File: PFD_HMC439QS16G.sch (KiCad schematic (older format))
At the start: 74 parts, among them J1 REF, J2 IN, J3 Error_Out, J4 C64AC, J5 Fast_Out, U1 HMC439QS16G, U2 LT3045EMSE, U3 LT3094EMSE, U4 ADA4896-2ARMZ, U5 ADA4896-2ARMZ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

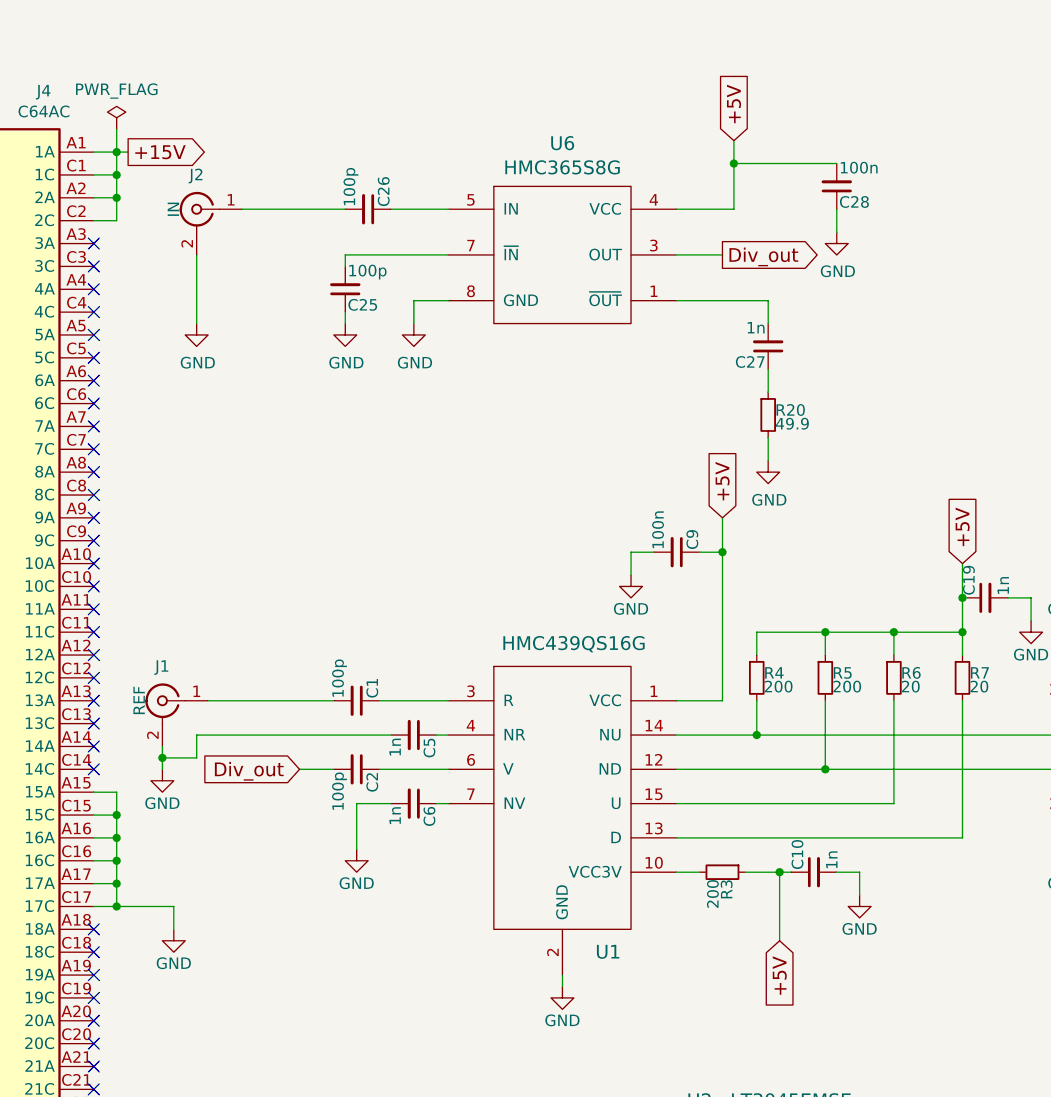
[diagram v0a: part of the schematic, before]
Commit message: Remove HMC365 frequency divider
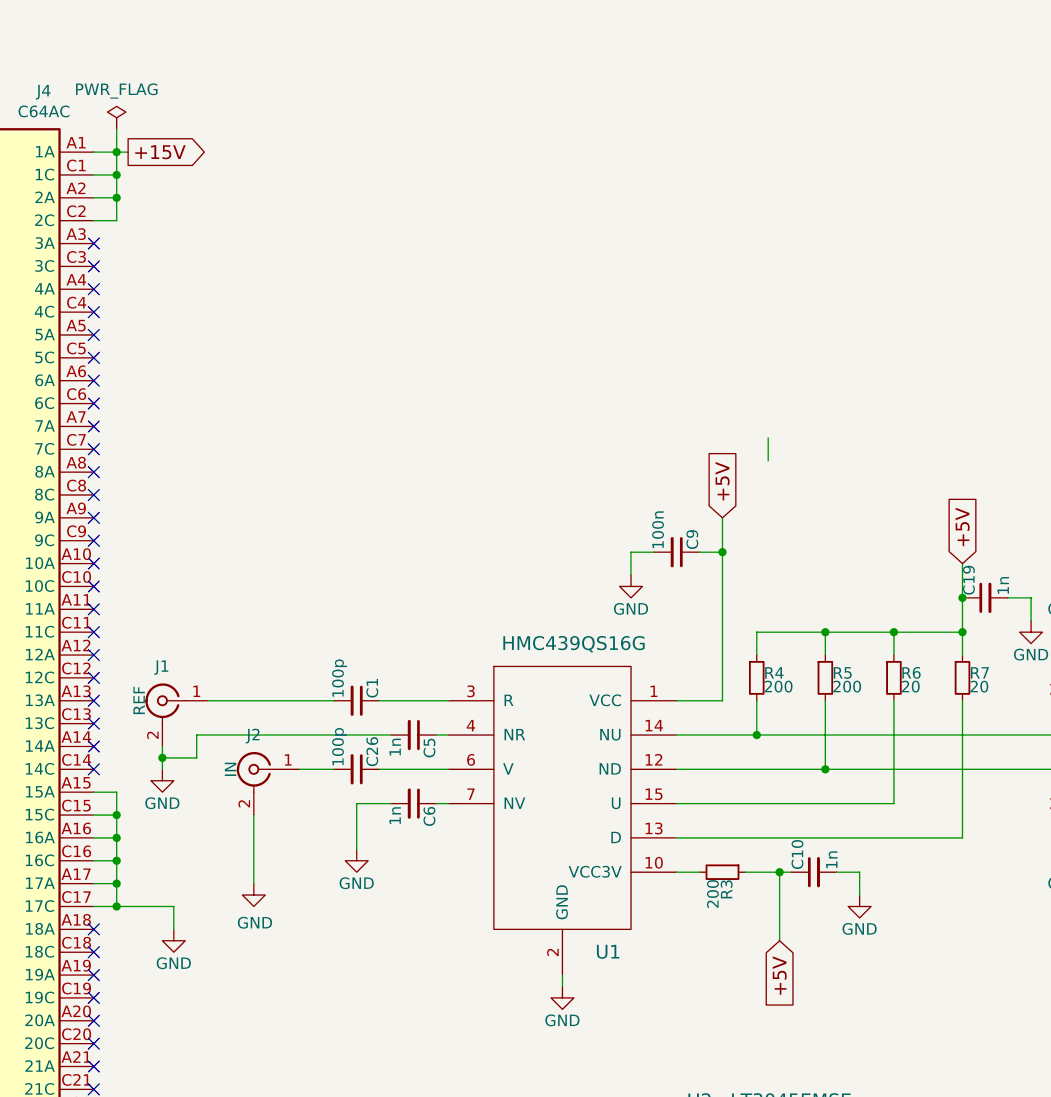
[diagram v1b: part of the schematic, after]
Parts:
- removed C2, C25: 100p, Capacitor_SMD:C_0402_1005Metric, symbol Device:C_Small
- removed C27: 1n, Capacitor_SMD:C_0603_1608Metric, symbol Device:C_Small
- removed C28: 100n, Capacitor_SMD:C_0603_1608Metric, symbol Device:C_Small
- removed R20: 49.9, Resistor_SMD:R_0603_1608Metric, symbol Device:R_Small
- removed U6: HMC365S8G, Package_SO:SOIC-8-1EP_3.9x4.9mm_P1.27mm_EP2.41x3.81mm, symbol Linear-Technology:HMC365S8G
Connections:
- net at U1.6 (V): now also C26.1
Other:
- moved on the sheet: C26, J2
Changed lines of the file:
@@
 Sheet 1 1
 Title "HMC439 Phase-Frequency Detector"
-Date "2021-03-18"
-Rev "1.2"
+Date "2021-08-22"
+Rev "1.2b"
 Comp "APQ"
 Comment1 "Tilman Preuschoff"
@@
 $EndComp
 $Comp
-L Device:C_Small C2
-U 1 1 5C6B19B9
-P 2150 3800
-F 0 "C2" H 2160 3870 50  0000 L CNN
-F 1 "100p" H 2160 3720 50  0000 L CNN
-F 2 "Capacitor_SMD:C_0402_1005Metric" H 2150 3800 50  0001 C CNN
-F 3 "" H 2150 3800 50  0001 C CNN
-	1    2150 3800
-	0    1    1    0
-$EndComp
-$Comp
 L Device:C_Small C6
 U 1 1 5C6B1ADB
@@
 L Connector:Conn_Coaxial J2
 U 1 1 5C6B26F6
-P 1450 1350
-F 0 "J2" H 1450 1500 50  0000 C CNN
-F 1 "IN" V 1550 1350 50  0000 C CNN
-F 2 "Connector_Coaxial:SMA_Amphenol_901-144_Vertical" H 1450 1350 50  0001 C CNN
-F 3 "" H 1450 1350 50  0001 C CNN
-	1    1450 1350
+P 1700 3800
+F 0 "J2" H 1700 3950 50  0000 C CNN
+F 1 "IN" V 1800 3800 50  0000 C CNN
+F 2 "Connector_Coaxial:SMA_Amphenol_901-144_Vertical" H 1700 3800 50  0001 C CNN
+F 3 "" H 1700 3800 50  0001 C CNN
+	1    1700 3800
 	-1   0    0    -1
 $EndComp
@@
 	9800 1300 9800 1900
 $Comp
-L Linear-Technology:HMC365S8G U6
-U 1 1 6058F7BE
-P 3050 1700
-F 0 "U6" H 3050 2337 60  0000 C CNN
-F 1 "HMC365S8G" H 3050 2231 60  0000 C CNN
-F 2 "Package_SO:SOIC-8-1EP_3.9x4.9mm_P1.27mm_EP2.41x3.81mm" H 3050 1700 60  0001 C CNN
-F 3 "https://www.analog.com/media/en/technical-documentation/data-sheets/HMC365S8G.pdf" H 3050 1700 60  0001 C CNN
-	1    3050 1700
-	1    0    0    -1
-$EndComp
-$Comp
 L Device:C_Small C26
 U 1 1 605ABF87
-P 2200 1350
-F 0 "C26" H 2210 1420 50  0000 L CNN
-F 1 "100p" H 2210 1270 50  0000 L CNN
-F 2 "Capacitor_SMD:C_0402_1005Metric" H 2200 1350 50  0001 C CNN
-F 3 "" H 2200 1350 50  0001 C CNN
-	1    2200 1350
+P 2150 3800
+F 0 "C26" H 2160 3870 50  0000 L CNN
+F 1 "100p" H 2160 3720 50  0000 L CNN
+F 2 "Capacitor_SMD:C_0402_1005Metric" H 2150 3800 50  0001 C CNN
+F 3 "" H 2150 3800 50  0001 C CNN
+	1    2150 3800
 	0    1    -1   0
-$EndComp
-$Comp
-L power:GND #PWR0105
-U 1 1 605AD690
-P 2400 1850
-F 0 "#PWR0105" H 2400 1600 50  0001 C CNN
-F 1 "GND" H 2405 1677 50  0000 C CNN
-F 2 "" H 2400 1850 50  0001 C CNN
-F 3 "" H 2400 1850 50  0001 C CNN
-	1    2400 1850
-	1    0    0    -1
-$EndComp
-$Comp
-L power:GND #PWR0106
-U 1 1 605ADE4E
-P 2100 1850
-F 0 "#PWR0106" H 2100 1600 50  0001 C CNN
-F 1 "GND" H 2105 1677 50  0000 C CNN
-F 2 "" H 2100 1850 50  0001 C CNN
-F 3 "" H 2100 1850 50  0001 C CNN
-	1    2100 1850
-	1    0    0    -1
 $EndComp
 $Comp
 L power:GND #PWR0110
 U 1 1 605BA26B
-P 1450 1850
-F 0 "#PWR0110" H 1450 1600 50  0001 C CNN
-F 1 "GND" H 1455 1677 50  0000 C CNN
-F 2 "" H 1450 1850 50  0001 C CNN
-F 3 "" H 1450 1850 50  0001 C CNN
-	1    1450 1850
-	1    0    0    -1
-$EndComp
-Wire Wire Line
-	1450 1550 1450 1850
-Wire Wire Line
-	2400 1750 2400 1850
-Wire Wire Line
-	2400 1750 2550 1750
-$Comp
-L Device:C_Small C25
-U 1 1 605DBB01
-P 2100 1700
-F 0 "C25" H 2110 1770 50  0000 L CNN
-F 1 "100p" H 2110 1620 50  0000 L CNN
-F 2 "Capacitor_SMD:C_0402_1005Metric" H 2100 1700 50  0001 C CNN
-F 3 "" H 2100 1700 50  0001 C CNN
-	1    2100 1700
-	1    0    0    1
-$EndComp
-Wire Wire Line
-	2550 1550 2100 1550
-Wire Wire Line
-	2100 1550 2100 1600
-Wire Wire Line
-	2100 1850 2100 1800
-Wire Wire Line
-	1650 1350 2100 1350
-Wire Wire Line
-	2300 1350 2550 1350
+P 1700 4300
+F 0 "#PWR0110" H 1700 4050 50  0001 C CNN
+F 1 "GND" H 1705 4127 50  0000 C CNN
+F 2 "" H 1700 4300 50  0001 C CNN
+F 3 "" H 1700 4300 50  0001 C CNN
+	1    1700 4300
+	1    0    0    -1
+$EndComp
+Wire Wire Line
+	1700 4000 1700 4300
 Wire Wire Line
 	1300 3700 1300 3750
@@
 Wire Wire Line
 	1300 3750 1300 3800
-Text GLabel 3800 1050 1    60   Input ~ 0
-+5V
-$Comp
-L Device:C_Small C28
-U 1 1 60639204
-P 4250 1250
-F 0 "C28" H 4260 1320 50  0000 L CNN
-F 1 "100n" H 4260 1170 50  0000 L CNN
-F 2 "Capacitor_SMD:C_0603_1608Metric" H 4250 1250 50  0001 C CNN
-F 3 "" H 4250 1250 50  0001 C CNN
-	1    4250 1250
-	1    0    0    1
-$EndComp
-Wire Wire Line
-	3800 1050 3800 1150
-Wire Wire Line
-	3800 1350 3550 1350
-Wire Wire Line
-	3800 1150 4250 1150
-Connection ~ 3800 1150
-Wire Wire Line
-	3800 1150 3800 1350
-$Comp
-L power:GND #PWR0111
-U 1 1 60661DA4
-P 4250 1450
-F 0 "#PWR0111" H 4250 1200 50  0001 C CNN
-F 1 "GND" H 4255 1277 50  0000 C CNN
-F 2 "" H 4250 1450 50  0001 C CNN
-F 3 "" H 4250 1450 50  0001 C CNN
-	1    4250 1450
-	1    0    0    -1
-$EndComp
-Wire Wire Line
-	4250 1350 4250 1450
-Text GLabel 3750 1550 2    60   Output ~ 0
-Div_out
-Wire Wire Line
-	3750 1550 3550 1550
-Text GLabel 1900 3800 0    60   Input ~ 0
-Div_out
 Wire Wire Line
 	2050 3800 1900 3800
@@
 Wire Wire Line
 	2150 3950 2150 4150
-$Comp
-L power:GND #PWR0113
-U 1 1 606F498E
-P 3950 2450
-F 0 "#PWR0113" H 3950 2200 50  0001 C CNN
-F 1 "GND" H 3955 2277 50  0000 C CNN
-F 2 "" H 3950 2450 50  0001 C CNN
-F 3 "" H 3950 2450 50  0001 C CNN
-	1    3950 2450
-	1    0    0    -1
-$EndComp
-$Comp
-L Device:C_Small C27
-U 1 1 606F5D57
-P 3950 1950
-F 0 "C27" H 3960 2020 50  0000 L CNN
-F 1 "1n" H 3960 1870 50  0000 L CNN
-F 2 "Capacitor_SMD:C_0603_1608Metric" H 3950 1950 50  0001 C CNN
-F 3 "" H 3950 1950 50  0001 C CNN
-	1    3950 1950
-	-1   0    0    1
-$EndComp
-$Comp
-L Device:R_Small R20
-U 1 1 606F85CF
-P 3950 2250
-F 0 "R20" H 3980 2270 50  0000 L CNN
-F 1 "49.9" H 3980 2210 50  0000 L CNN
-F 2 "Resistor_SMD:R_0603_1608Metric" H 3950 2250 50  0001 C CNN
-F 3 "" H 3950 2250 50  0001 C CNN
-	1    3950 2250
-	1    0    0    -1
-$EndComp
-Wire Wire Line
-	3950 1750 3950 1850
-Wire Wire Line
-	3550 1750 3950 1750
-Wire Wire Line
-	3950 2150 3950 2050
 Wire Wire Line
 	3950 2450 3950 2350
